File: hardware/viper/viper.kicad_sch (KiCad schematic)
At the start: 307 parts, among them J1 TYPE-C-31-M-12, Q1 2N7002, SW1 Cherry Alps Hybrid, SW10 Cherry Alps Hybrid, SW11 Cherry Alps Hybrid, SW12 Cherry Alps Hybrid, SW13 Cherry Alps Hybrid, SW14 Cherry Alps Hybrid, SW14_1 Cherry Alps Hybrid, SW15 Cherry Alps Hybrid, SW16 Cherry Alps Hybrid, SW17 Cherry Alps Hybrid, SW18 Cherry Alps Hybrid, SW19 Cherry Alps Hybrid, SW2 Cherry Alps Hybrid, SW20 Cherry Alps Hybrid, SW21 Cherry Alps Hybrid, SW22 Cherry Alps Hybrid, SW23 Cherry Alps Hybrid, SW24 Cherry Alps Hybrid, SW25 Cherry Alps Hybrid, SW26 Cherry Alps Hybrid, SW27 Cherry Alps Hybrid, SW28 Cherry Alps Hybrid, SW28_1 Cherry Alps Hybrid, SW29 Cherry Alps Hybrid, SW29_1 Cherry Alps Hybrid, SW3 Cherry Alps Hybrid, SW30 Cherry Alps Hybrid, SW31 Cherry Alps Hybrid, SW32 Cherry Alps Hybrid, SW33 Cherry Alps Hybrid, SW34 Cherry Alps Hybrid, SW35 Cherry Alps Hybrid, SW36 Cherry Alps Hybrid, SW37 Cherry Alps Hybrid, SW38 Cherry Alps Hybrid, SW39 Cherry Alps Hybrid, SW4 Cherry Alps Hybrid, SW40 Cherry Alps Hybrid, SW41 Cherry Alps Hybrid, SW41_1 Cherry Alps Hybrid, SW42 Cherry Alps Hybrid, SW43 Cherry Alps Hybrid, SW43_1 Cherry Alps Hybrid, SW44 Cherry Alps Hybrid, SW45 Cherry Alps Hybrid, SW46 Cherry Alps Hybrid, SW47 Cherry Alps Hybrid, SW48 Cherry Alps Hybrid, SW49 Cherry Alps Hybrid, SW5 Cherry Alps Hybrid, SW50 Cherry Alps Hybrid, SW51 Cherry Alps Hybrid, SW52 Cherry Alps Hybrid, SW53 Cherry Alps Hybrid, SW54 Cherry Alps Hybrid, SW55 Cherry Alps Hybrid, SW55_1 Cherry Alps Hybrid, SW56 Cherry Alps Hybrid, SW57 Cherry Alps Hybrid, SW58 Cherry Alps Hybrid, SW59 Cherry Alps Hybrid, SW6 Cherry Alps Hybrid, SW60 Cherry Alps Hybrid, SW61 Cherry Alps Hybrid, SW7 Cherry Alps Hybrid, SW8 Cherry Alps Hybrid, SW9 Cherry Alps Hybrid, U1 USBLC6-2SC6, U2 ATmega32U4-A, Y1 16MHz

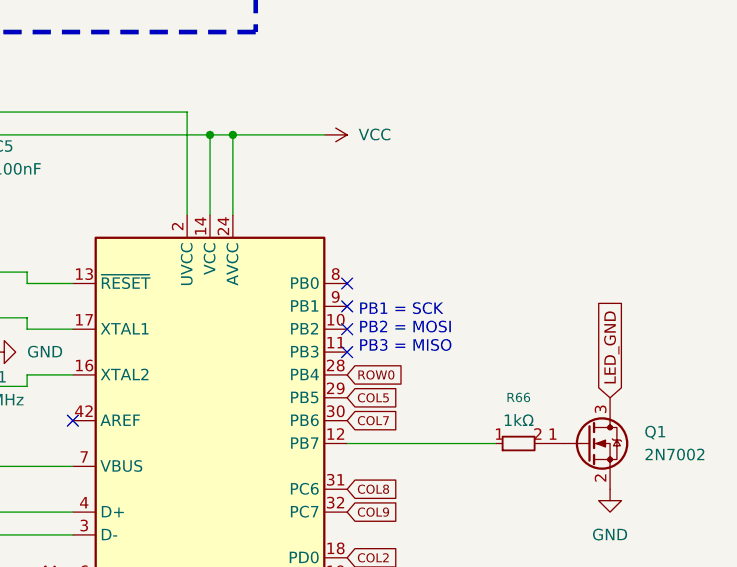
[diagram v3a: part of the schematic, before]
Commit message: Attach CAPS_LED
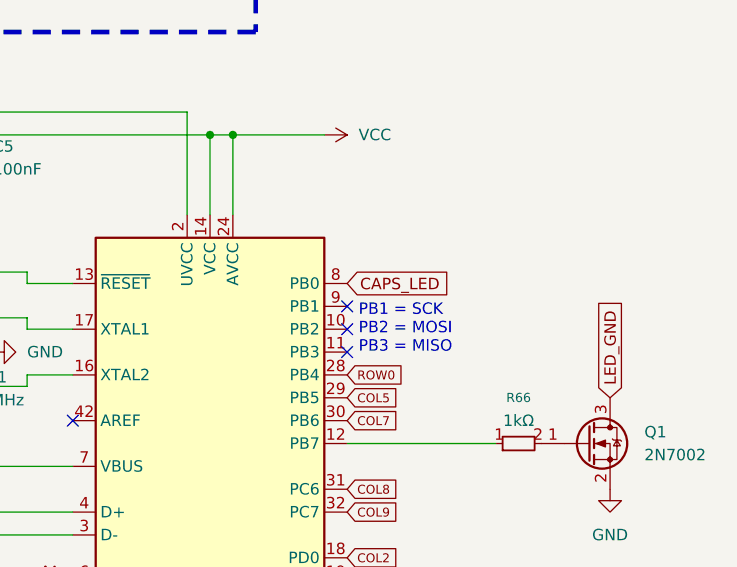
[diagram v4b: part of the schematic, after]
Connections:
- net CAPS_LED: now also U2.8 (PB0)
- no-connect marks 8 -> 7
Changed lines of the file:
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@@
 	)
 	(no_connect
-		(at 429.26 142.24)
-	)
-	(no_connect
 		(at 398.78 157.48)
 	)
@@
 				(hide yes)
 			)
+		)
+	)
+	(global_label "CAPS_LED"
+		(shape input)
+		(at 429.26 142.24 0)
+		(fields_autoplaced yes)
+		(effects
+			(font
+				(size 1.27 1.27)
+			)
+			(justify left)
+		)
+		(property "Intersheetrefs" "${INTERSHEET_REFS}"
+			(at 441.498 142.24 0)
+			(effects
+				(font
+					(size 1.27 1.27)
+				)
+				(justify left)
+				(hide yes)
+			)

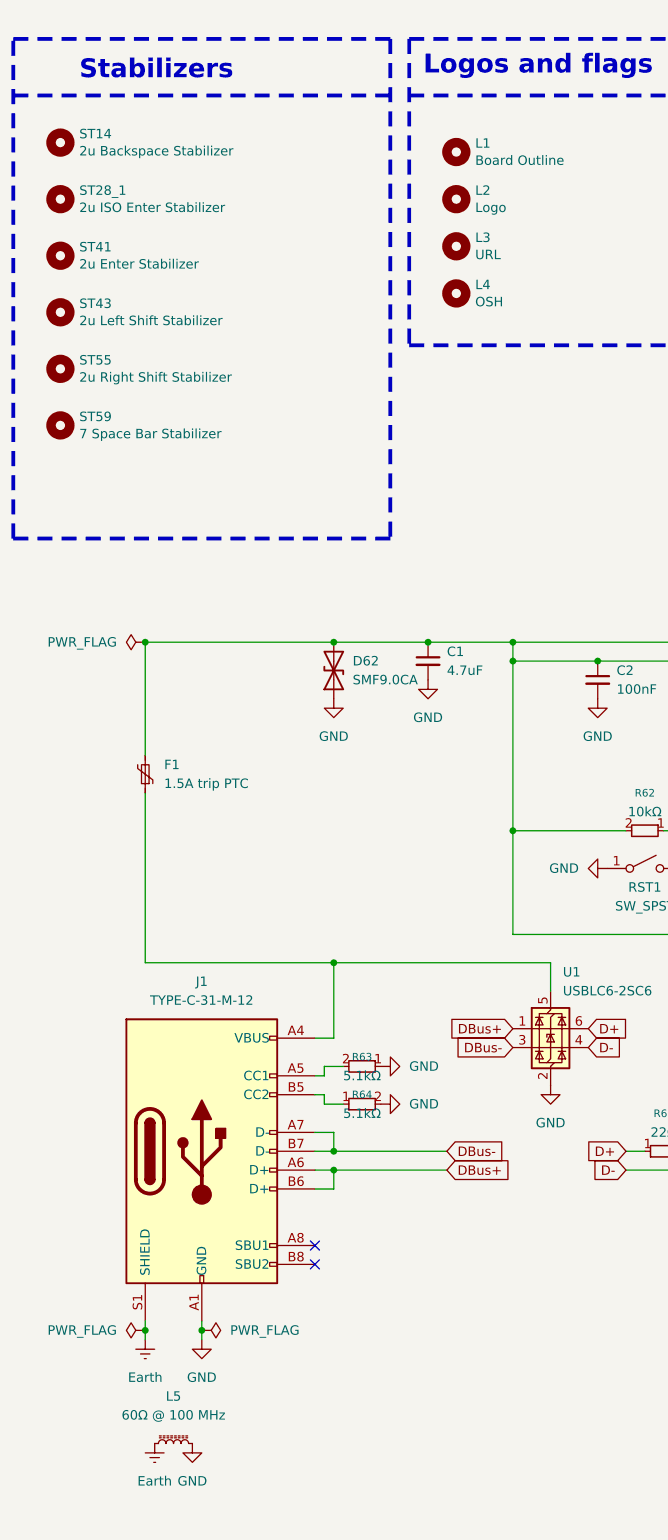
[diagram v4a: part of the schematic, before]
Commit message: Manually corrected split-hhkb layout
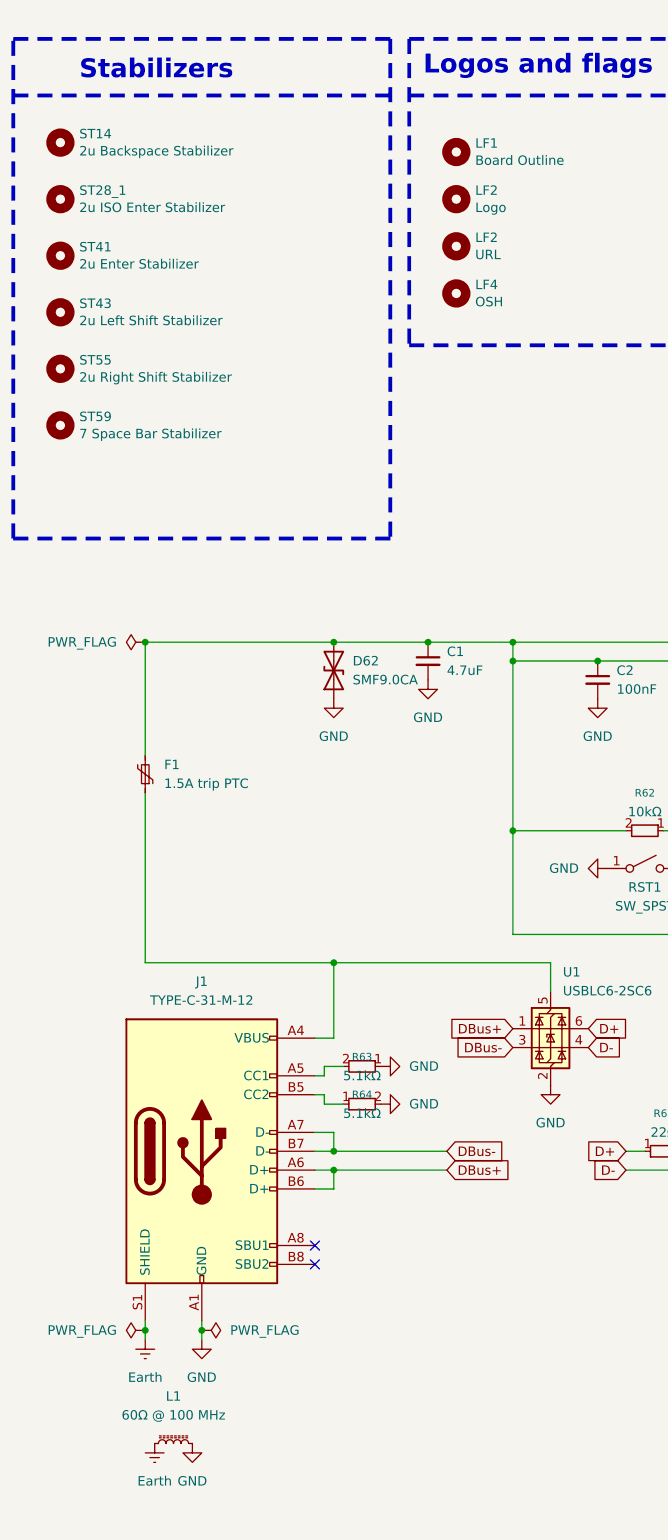
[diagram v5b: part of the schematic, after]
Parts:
- renumbered L5 to L1, L1 to LF1, L2 to LF2, L3 to LF2, L4 to LF4
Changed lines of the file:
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@@
 		(on_board yes)
 		(dnp no)
-		(property "Reference" "L1"
+		(property "Reference" "LF1"
 			(at 336.55 55.9816 0)
 			(effects
@@
 			(project "viper"
 				(path "/9e45a776-7007-48ff-b543-dc98423173b7"
-					(reference "L1")
+					(reference "LF1")
 					(unit 1)
 				)
@@
 		(on_board yes)
 		(dnp no)
-		(property "Reference" "L2"
+		(property "Reference" "LF2"
 			(at 336.55 62.3316 0)
 			(effects
@@
 			(project "viper"
 				(path "/9e45a776-7007-48ff-b543-dc98423173b7"
-					(reference "L2")
+					(reference "LF2")
 					(unit 1)
 				)
@@
 		(dnp no)
 		(fields_autoplaced yes)
-		(property "Reference" "L5"
+		(property "Reference" "L1"
 			(at 295.91 224.79 90)
 			(effects
@@
 			(project "viper"
 				(path "/9e45a776-7007-48ff-b543-dc98423173b7"
-					(reference "L5")
+					(reference "L1")
 					(unit 1)
 				)
@@
 		(on_board yes)
 		(dnp no)
-		(property "Reference" "L4"
+		(property "Reference" "LF4"
 			(at 336.55 75.0316 0)
 			(effects
@@
 			(project "viper"
 				(path "/9e45a776-7007-48ff-b543-dc98423173b7"
-					(reference "L4")
+					(reference "LF4")
 					(unit 1)
 				)
@@
 		(on_board yes)
 		(dnp no)
-		(property "Reference" "L3"
+		(property "Reference" "LF2"
 			(at 336.55 68.6816 0)
 			(effects
@@
 			(project "viper"
 				(path "/9e45a776-7007-48ff-b543-dc98423173b7"
-					(reference "L3")
+					(reference "LF2")
 					(unit 1)
 				)

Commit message: Test with voyager60 pinout & kle2netlist
Mock positions for rgb leds & ferrite bead

Unrouted board with kle2netlist & pos2orient

No per-switch leds yet

Append docker build to existing schematic

Update schematic from PCB

Apply pos2orient file

Add led matrix sheet, marked as DNP

Use Switch_Misc/MX-LED-PolarityMarked in layout2ledschematic job

Disable unneeded symbol/footprint libraries

Added mock mxlockled symbol, dnp

MX-Lock-LED based on MX-LED from ai03-2725/MX_V2

Fixed courtyard of W_Hybrid_Cherry_MX_Alps_1.00u

Started flipping switch symbols for better routing
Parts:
- removed C2: 100nF, Capacitor_SMD:C_0805_2012Metric_Pad1.18x1.45mm_HandSolder, symbol Device:C_Small
- removed D1, D10, D11, D12, D13, D14, D15, D16, D17, D18, D19, D2, D20, D21, D22, D23, D24, D25, D26, D27, D28, D29, D3, D30, D31, D32, D33, D34, D35, D36, D37, D38, D39, D4, D40, D41, D42, D43, D44, D45, D46, D47, D48, D49, D5, D50, D51, D52, D53, D54, D55, D56, D57, D58, D59, D6, D60, D61, D7, D8, D9: 1N4148, Diode_SMD:D_0805_2012Metric_Pad1.15x1.40mm_HandSolder, symbol Device:D_Small
- removed D62: SMF9.0CA, Diode_SMD:D_0805_2012Metric_Pad1.15x1.40mm_HandSolder, symbol Device:D_TVS
- removed LED1, LED10, LED11, LED12, LED13, LED14, LED14_1, LED15, LED16, LED17, LED18, LED19, LED2, LED20, LED21, LED22, LED23, LED24, LED25, LED26, LED27, LED28, LED28_1, LED29, LED29_1, LED3, LED30, LED31, LED32, LED33, LED34, LED35, LED36, LED37, LED38, LED39, LED4, LED40, LED41, LED41_1, LED42, LED43, LED43_1, LED44, LED45, LED46, LED47, LED48, LED49, LED5, LED50, LED51, LED52, LED53, LED54, LED55, LED55_1, LED56, LED57, LED58, LED59, LED6, LED60, LED61, LED7, LED8, LED9: LED, Switch_Misc:MX-LED-PolarityMarked, symbol Device:LED_Small
- removed R1, R10, R11, R12, R13, R14, R15, R16, R17, R18, R19, R2, R20, R21, R22, R23, R24, R25, R26, R27, R28, R29, R3, R30, R31, R32, R33, R34, R35, R36, R37, R38, R39, R4, R40, R41, R42, R43, R44, R45, R46, R47, R48, R49, R5, R50, R51, R52, R53, R54, R55, R56, R57, R58, R59, R6, R60, R61, R7, R8, R9: 470Ω, Resistor_SMD:R_0815_2038Metric_Pad1.20x4.05mm_HandSolder, symbol Device:R_Small
- removed R62: 10kΩ, Resistor_SMD:R_0805_2012Metric_Pad1.20x1.40mm_HandSolder, symbol Device:R_Small
- removed SW1, SW10, SW11, SW12, SW13, SW14_1, SW16, SW17, SW18, SW19, SW2, SW20, SW21, SW22, SW23, SW24, SW25, SW26, SW27, SW28_1, SW3, SW30, SW31, SW32, SW33, SW34, SW35, SW36, SW37, SW38, SW39, SW4, SW40, SW41_1, SW42, SW44, SW45, SW46, SW47, SW48, SW49, SW5, SW50, SW51, SW52, SW53, SW54, SW56, SW57, SW6, SW61, SW7, SW8, SW9: Cherry Alps Hybrid, PCM_Switch_Keyboard_Hybrid:SW_Hybrid_Cherry_MX_Alps_1.00u, symbol Switch:SW_Push_45deg
- removed SW14: Cherry Alps Hybrid, PCM_Switch_Keyboard_Hybrid:SW_Hybrid_Cherry_MX_Alps_2.00u, symbol Switch:SW_Push_45deg
- removed SW15, SW28, SW58, SW60: Cherry Alps Hybrid, PCM_Switch_Keyboard_Hybrid:SW_Hybrid_Cherry_MX_Alps_1.50u, symbol Switch:SW_Push_45deg
- removed SW29, SW55_1: Cherry Alps Hybrid, PCM_Switch_Keyboard_Hybrid:SW_Hybrid_Cherry_MX_Alps_1.75u, symbol Switch:SW_Push_45deg
- removed SW29_1, SW43_1: Cherry Alps Hybrid, PCM_Switch_Keyboard_Hybrid:SW_Hybrid_Cherry_MX_Alps_1.25u, symbol Switch:SW_Push_45deg
- removed SW41, SW43: Cherry Alps Hybrid, PCM_Switch_Keyboard_Hybrid:SW_Hybrid_Cherry_MX_Alps_2.25u, symbol Switch:SW_Push_45deg
- removed SW55: Cherry Alps Hybrid, PCM_Switch_Keyboard_Hybrid:SW_Hybrid_Cherry_MX_Alps_2.75u, symbol Switch:SW_Push_45deg
- removed SW59: Cherry Alps Hybrid, PCM_Switch_Keyboard_Hybrid:SW_Hybrid_Cherry_MX_Alps_7.00u, symbol Switch:SW_Push_45deg
- added D63: SMF9.0CA, Diode_SMD:D_SOD-123, symbol Device:D_Zener_Small
- added R66: 10k, Resistor_SMD:R_0603_1608Metric, symbol Device:R_Small
- added ST59_1: 8u Space Bar Stabilizer, PCM_Mounting_Keyboard_Stabilizer:Stabilizer_Cherry_MX_8.00u, symbol Mechanical:MountingHole
- added ST60: 3u Left Split HHKB Stabilizer, Mounting_Keyboard_Stabilizer:Stabilizer_Cherry_MX_3.00u, symbol Mechanical:MountingHole
- C1: renamed from C7; value 22pF -> 22p; footprint Capacitor_SMD:C_0805_2012Metric_Pad1.18x1.45mm_HandSolder -> Capacitor_SMD:C_0603_1608Metric
- C2: renamed from C6; value 22pF -> 22p; footprint Capacitor_SMD:C_0805_2012Metric_Pad1.18x1.45mm_HandSolder -> Capacitor_SMD:C_0603_1608Metric
- C3, C4, C5: footprint Capacitor_SMD:C_0805_2012Metric_Pad1.18x1.45mm_HandSolder -> Capacitor_SMD:C_0603_1608Metric
- C6: renamed from C1; value 4.7uF -> 10u; footprint Capacitor_SMD:C_0805_2012Metric_Pad1.18x1.45mm_HandSolder -> Capacitor_SMD:C_0603_1608Metric
- C7: renamed from C8; value 1uF -> 1u; footprint Capacitor_SMD:C_0805_2012Metric_Pad1.18x1.45mm_HandSolder -> Capacitor_SMD:C_0603_1608Metric
- F1: footprint Fuse:Fuse_0805_2012Metric_Pad1.15x1.40mm_HandSolder -> Fuse:Fuse_1206_3216Metric
- R63: renamed from R65; value 22Ω -> 22; footprint Resistor_SMD:R_0805_2012Metric_Pad1.20x1.40mm_HandSolder -> Resistor_SMD:R_0603_1608Metric
- R64: renamed from R67; value 22Ω -> 22; footprint Resistor_SMD:R_0805_2012Metric_Pad1.20x1.40mm_HandSolder -> Resistor_SMD:R_0603_1608Metric
- R65: renamed from R68; value 1kΩ -> 10k; footprint Resistor_SMD:R_0805_2012Metric_Pad1.20x1.40mm_HandSolder -> Resistor_SMD:R_0603_1608Metric
- R69: renamed from R66; value 1kΩ -> 1k; footprint Resistor_SMD:R_0815_2038Metric_Pad1.20x4.05mm_HandSolder -> Resistor_SMD:R_0805_2012Metric
- RCC1: renamed from R63; value 5.1kΩ -> 5.1k; footprint Resistor_SMD:R_0805_2012Metric_Pad1.20x1.40mm_HandSolder -> Resistor_SMD:R_0603_1608Metric
- RCC2: renamed from R64; value 5.1kΩ -> 5.1k; footprint Resistor_SMD:R_0805_2012Metric_Pad1.20x1.40mm_HandSolder -> Resistor_SMD:R_0603_1608Metric
- ST14, ST43: footprint PCM_Mounting_Keyboard_Stabilizer:Stabilizer_Cherry_MX_2.00u -> Mounting_Keyboard_Stabilizer:Stabilizer_Cherry_MX_2.00u; now left out of the parts list
- ST42: renamed from ST41; footprint PCM_Mounting_Keyboard_Stabilizer:Stabilizer_Cherry_MX_2.00u -> Mounting_Keyboard_Stabilizer:Stabilizer_Cherry_MX_2.00u; now left out of the parts list
- ST54: renamed from ST55; footprint PCM_Mounting_Keyboard_Stabilizer:Stabilizer_Cherry_MX_2.00u -> Mounting_Keyboard_Stabilizer:Stabilizer_Cherry_MX_2.00u; now left out of the parts list
- ST58: renamed from ST28_1; value 2u ISO Enter Stabilizer -> 3u Left Split HHKB Stabilizer; footprint PCM_Mounting_Keyboard_Stabilizer:Stabilizer_Cherry_MX_2.00u -> Mounting_Keyboard_Stabilizer:Stabilizer_Cherry_MX_3.00u; now left out of the parts list
- ST59: value 7 Space Bar Stabilizer -> 7u Space Bar Stabilizer; footprint PCM_Mounting_Keyboard_Stabilizer:Stabilizer_Cherry_MX_7.00u -> Mounting_Keyboard_Stabilizer:Stabilizer_Cherry_MX_7.00u; now left out of the parts list
- renumbered LF2 to LF3, U2 to U1, U1 to U2
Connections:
- net USB+ is gone; now on net D+: R63.2, U1.4 (D+)
- net USB- is gone; now on net D-: R64.2, U1.3 (D-)
- net COL0: now also U1.39 (PF4); no longer U1.20 (PD2)
- net COL1: now also U1.36 (PF7); no longer U1.19 (PD1)
- net COL10: now also U1.26 (PD6); no longer U1.40 (PF1)
- net COL11: now also U1.25 (PD4); no longer U1.39 (PF4)
- net COL12: now also U1.22 (PD5); no longer U1.38 (PF5)
- net COL13: now also U1.21 (PD3); no longer U1.37 (PF6)
- net COL2: now also U1.38 (PF5); no longer U1.18 (PD0)
- net COL3: now also U1.37 (PF6); no longer U1.21 (PD3)
- net COL4: now also U1.32 (PC7); no longer U1.22 (PD5)
- net COL5: now also U1.31 (PC6); no longer U1.29 (PB5)
- net COL6: now also U1.30 (PB6); no longer U1.41 (PF0)
- net COL7: now also U1.29 (PB5); no longer U1.30 (PB6)
- net COL8: now also U1.28 (PB4); no longer U1.31 (PC6)
- net COL9: now also U1.27 (PD7); no longer U1.32 (PC7)
- net D+: now also J1.A6 (D+), J1.B6 (D+), R64.1, U2.3 (I/O2), U2.4 (I/O2); no longer R63.1, U2.6 (I/O1)
- net D-: now also J1.A7 (D-), J1.B7 (D-), R63.1, U2.1 (I/O1), U2.6 (I/O1); no longer R64.1, U2.4 (I/O2)
- net GND: now also D63.2 (A)
- net RGB_LED: now also U1.20 (PD2); no longer U1.36 (PF7)
- net ROW0: now also U1.9 (PB1); no longer U1.28 (PB4)
- net ROW1: now also U1.10 (PB2); no longer U1.27 (PD7)
- net ROW2: now also U1.11 (PB3); no longer U1.26 (PD6)
- net ROW3: now also U1.41 (PF0); no longer U1.25 (PD4)
- net ROW4: now also U1.40 (PF1); no longer U1.1 (PE6)
- net VCC: now also D63.1 (K), R66.2
- net VBUS: now reaches F1.1, J1.A4 (VBUS), J1.A9 (VBUS), J1.B4 (VBUS), J1.B9 (VBUS), U2.5 (VBUS)
- net N$86: now reaches J1.B5 (CC2), RCC2.1
- net SWITCH_LED: now reaches R69.1, U1.12 (PB7)
- net ~{RESET}: now reaches RST1.2 (B), U1.13 (~{RESET})
- net ~{RESET}: now also R66.1
- net XTAL2: now reaches C1.1, U1.16 (XTAL2), Y1.3
- net XTAL1: now reaches C2.1, U1.17 (XTAL1), Y1.1
- net PE2: now reaches R65.1, U1.33 (~{HWB}/PE2)
- net UCAP: now reaches C7.1, U1.6 (UCAP)
- net N$85: now reaches J1.A5 (CC1), RCC1.2
- removed net DBus+: J1.A6 (D+), J1.B6 (D+), U2.1 (I/O1)
- removed net DBus-: J1.A7 (D-), J1.B7 (D-), U2.3 (I/O2)
- new net COL14: U1.19 (PD1)
- no-connect marks 7 -> 6
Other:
- added sheet LED-Matrix (viper-led-matrix.kicad_sch)
- added sheet Switch-Matrix (viper-switch-matrix.kicad_sch)
- note removed: "PB1 = SCK PB2 = MOSI PB3 = MISO"
- moved on the sheet: C1, C2, C3, C4, C5, C6, C7, CRGB1, CRGB2, CRGB3, CRGB4, F1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
